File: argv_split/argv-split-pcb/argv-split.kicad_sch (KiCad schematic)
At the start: 160 parts, among them SW1 SW_Push, SW10 SW_Push, SW11 SW_Push, SW12 SW_Push, SW13 SW_Push, SW14 SW_Push, SW15 SW_Push, SW16 SW_Push, SW17 SW_Push, SW18 SW_Push, SW19 SW_Push, SW2 SW_Push, SW20 SW_Push, SW21 SW_Push, SW22 SW_Push, SW23 SW_Push, SW24 SW_Push, SW25 SW_Push, SW26 SW_Push, SW27 SW_Push, SW28 SW_Push, SW29 SW_Push, SW3 SW_Push, SW30 SW_Push, SW31 SW_Push, SW32 SW_Push, SW33 SW_Push, SW34 SW_Push, SW35 SW_Push, SW36 SW_Push, SW37 SW_Push, SW38 SW_Push, SW39 SW_Push, SW4 SW_Push, SW40 SW_Push, SW41 SW_Push, SW42 SW_Push, SW43 SW_Push, SW44 SW_Push, SW45 SW_Push, SW46 SW_Push, SW47 SW_Push, SW48 SW_Push, SW49 SW_Push, SW5 SW_Push, SW50 SW_Push, SW51 SW_Push, SW52 SW_Push, SW53 SW_Push, SW54 SW_Push, SW55 SW_Push, SW56 SW_Push, SW57 SW_Push, SW58 SW_Push, SW59 SW_Push, SW6 SW_Push, SW60 SW_Push, SW61 SW_Push, SW62 SW_Push, SW63 SW_Push, SW64 SW_Push, SW65 SW_Push, SW66 SW_Push, SW67 SW_Push, SW68 SW_Push, SW69 SW_Push, SW7 SW_Push, SW70 SW_Push, SW71 SW_Push, SW72 SW_Push, SW73 SW_Push, SW74 SW_Push, SW75 SW_Push, SW76 SW_Push, SW8 SW_Push, SW9 SW_Push

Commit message: feat: layout pcb
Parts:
- D1, D10, D11, D12, D13, D14, D15, D16, D17, D18, D19, D2, D20, D21, D22, D23, D24, D25, D26, D27, D28, D29, D3, D30, D31, D32, D33, D34, D35, D36, D37, D38, D39, D4, D40, D41, D42, D43, D44, D45, D46, D47, D48, D49, D5, D50, D51, D52, D53, D54, D55, D56, D57, D58, D59, D6, D60, D61, D62, D63, D64, D65, D66, D67, D68, D69, D7, D70, D71, D72, D73, D74, D75, D76, D8, D9: footprint Diode_SMD:D_SOD-123 -> Diode_THT:D_DO-35_SOD27_P7.62mm_Horizontal
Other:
- moved on the sheet: D39, D40, D41, D42, D43, D44, D45, D46, D47, D48, D49, D50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

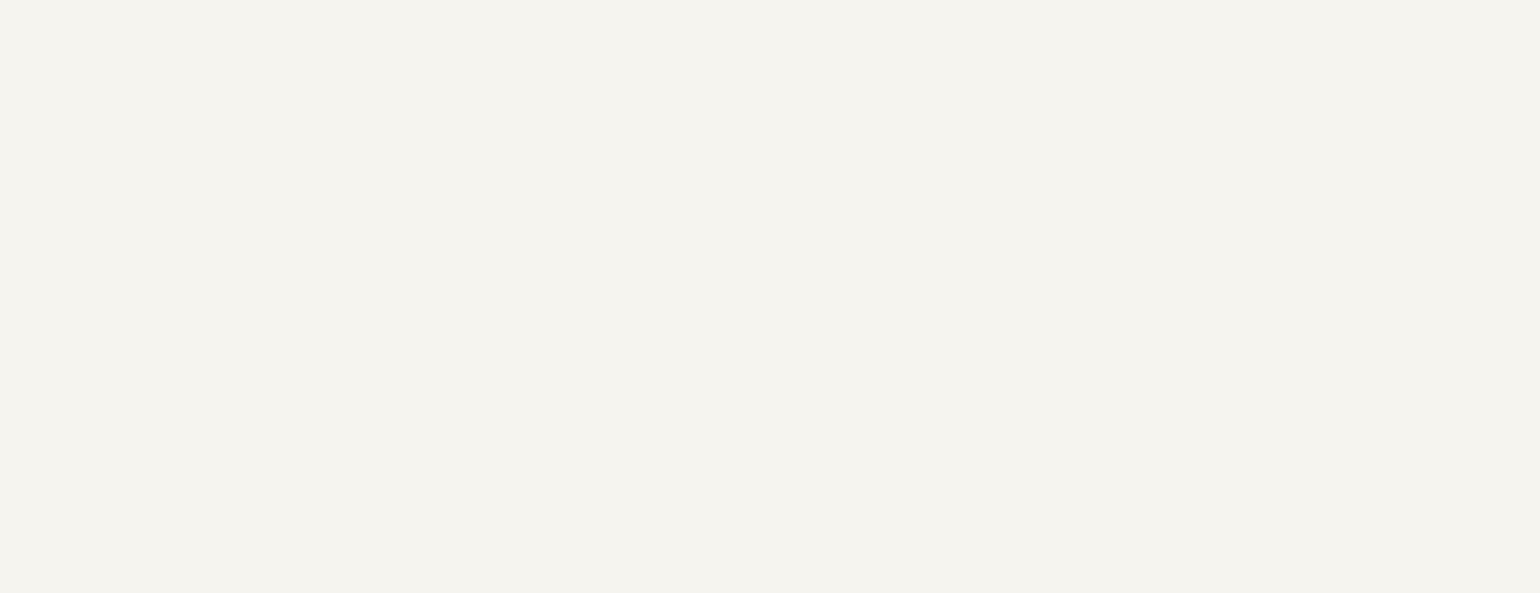
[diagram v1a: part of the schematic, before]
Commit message: feat(split): routing
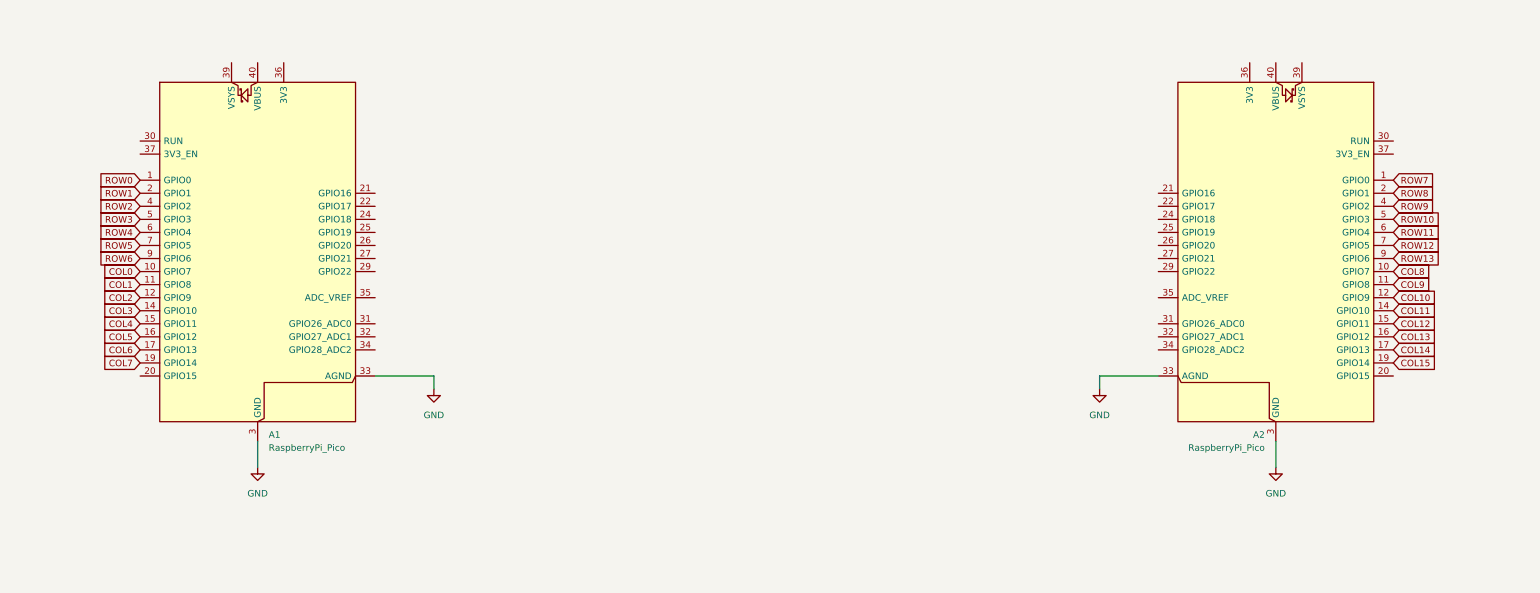
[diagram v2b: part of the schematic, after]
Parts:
- added A1, A2: RaspberryPi_Pico, Module:RaspberryPi_Pico_Common_Unspecified, symbol MCU_Module:RaspberryPi_Pico
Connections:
- net COL0: now also A1.10 (GPIO7)
- net COL1: now also A1.11 (GPIO8)
- net COL10: now also A2.12 (GPIO9)
- net COL11: now also A2.14 (GPIO10)
- net COL12: now also A2.15 (GPIO11)
- net COL13: now also A2.16 (GPIO12)
- net COL14: now also A2.17 (GPIO13)
- net COL15: now also A2.19 (GPIO14)
- net COL2: now also A1.12 (GPIO9)
- net COL3: now also A1.14 (GPIO10)
- net COL4: now also A1.15 (GPIO11)
- net COL5: now also A1.16 (GPIO12)
- net COL6: now also A1.17 (GPIO13)
- net COL7: now also A1.19 (GPIO14)
- net COL8: now also A2.10 (GPIO7)
- net COL9: now also A2.11 (GPIO8)
- net ROW0: now also A1.1 (GPIO0)
- net ROW1: now also A1.2 (GPIO1)
- net ROW10: now also A2.5 (GPIO3)
- net ROW11: now also A2.6 (GPIO4)
- net ROW12: now also A2.7 (GPIO5)
- net ROW13: now also A2.9 (GPIO6)
- net ROW2: now also A1.4 (GPIO2)
- net ROW3: now also A1.5 (GPIO3)
- net ROW4: now also A1.6 (GPIO4)
- net ROW5: now also A1.7 (GPIO5)
- net ROW6: now also A1.9 (GPIO6)
- net ROW7: now also A2.1 (GPIO0)
- net ROW8: now also A2.2 (GPIO1)
- net ROW9: now also A2.4 (GPIO2)
- new net GND: A1.13 (GND), A1.18 (GND), A1.23 (GND), A1.28 (GND), A1.3 (GND), A1.33 (AGND), A1.38 (GND), A1.8 (GND), A2.13 (GND), A2.18 (GND), A2.23 (GND), A2.28 (GND), A2.3 (GND), A2.33 (AGND), A2.38 (GND), A2.8 (GND)
